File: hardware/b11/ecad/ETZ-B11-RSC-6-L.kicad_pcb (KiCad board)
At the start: 2 copper layers, 112.3 x 85.8 mm, 0 parts

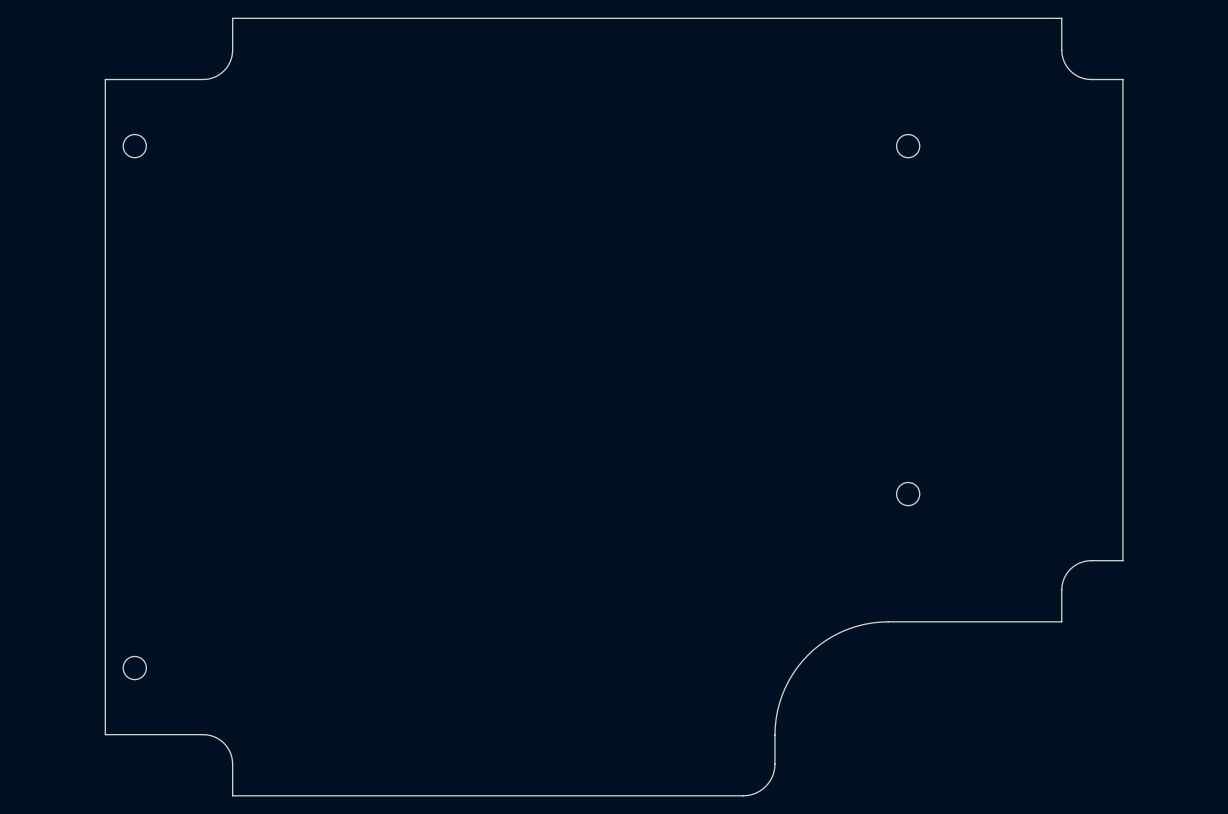
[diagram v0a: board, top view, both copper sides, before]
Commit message: fix(hardware/b11): correct 6-col PCB outlines and regenerate all boards
Update DXF outlines for all 6-col variants (LSC, RSC, LSP, RSP — both
normal and low profile) exported manually from OnShape with the _6
configuration. Regenerate all 16 KiCad PCBs from the corrected outlines
and re-place MX hotswap switches on the 4 normal-profile carrier boards.

Co-Authored-By: Claude Sonnet 4.6 <noreply@anthropic.com>
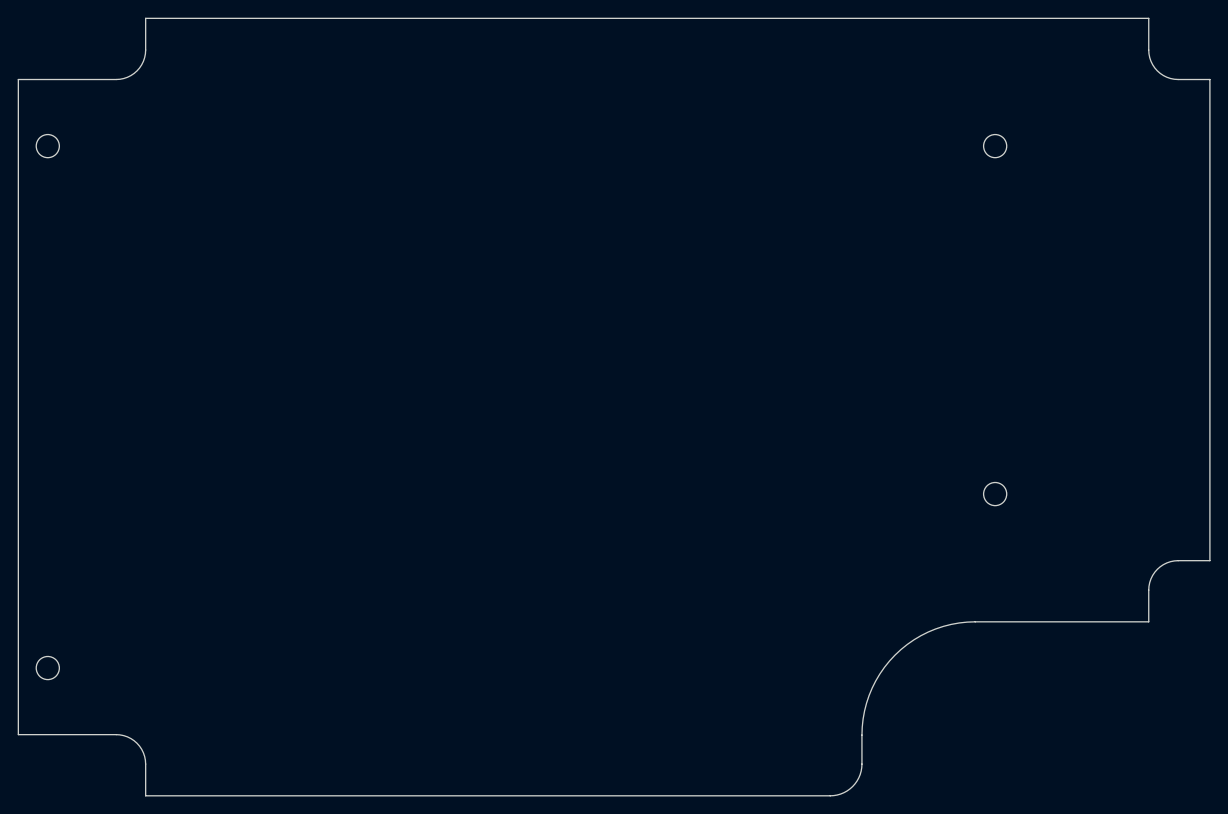
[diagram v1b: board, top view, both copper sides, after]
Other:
- board size 112.3 x 85.8 mm -> 131.5 x 85.8 mm
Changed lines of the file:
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@@
 		(allow_soldermask_bridges_in_footprints no)
 		(tenting front back)
-		(grid_origin 190.55 73.3)
+		(grid_origin 200.15 73.3)
 		(pcbplotparams
 			(layerselection 0x00000000_00000000_55555555_5755f5ff)
@@
 	)
 	(net 0 "")
-	(gr_circle
-		(center 180.949999 111.7)
-		(end 182.224999 111.7)
-		(stroke
-			(width 0.05)
-			(type default)
-		)
-		(fill no)
-		(layer "Edge.Cuts")
-	)
-	(gr_line
-		(start 106.399999 59.2)
-		(end 197.899999 59.2)
-		(stroke
-			(width 0.05)
-			(type default)
-		)
-		(layer "Edge.Cuts")
-	)
-	(gr_line
-		(start 204.65 65.95)
-		(end 204.65 119.05)
-		(stroke
-			(width 0.05)
-			(type default)
-		)
-		(layer "Edge.Cuts")
-	)
-	(gr_line
-		(start 197.899999 122.3)
-		(end 197.899999 125.8)
-		(stroke
-			(width 0.05)
-			(type default)
-		)
-		(layer "Edge.Cuts")
-	)
-	(gr_line
-		(start 103.15 138.25)
-		(end 92.35 138.25)
-		(stroke
-			(width 0.05)
-			(type default)
-		)
-		(layer "Edge.Cuts")
-	)
-	(gr_arc
-		(start 197.899999 122.3)
-		(mid 198.851902 120.001903)
-		(end 201.149999 119.05)
-		(stroke
-			(width 0.05)
-			(type default)
-		)
-		(layer "Edge.Cuts")
-	)
-	(gr_line
-		(start 92.35 138.25)
-		(end 92.35 65.95)
-		(stroke
-			(width 0.05)
-			(type default)
-		)
-		(layer "Edge.Cuts")
-	)
-	(gr_line
-		(start 201.149999 65.95)
-		(end 204.65 65.95)
-		(stroke
-			(width 0.05)
-			(type default)
-		)
-		(layer "Edge.Cuts")
-	)
-	(gr_arc
-		(start 106.4 62.7)
-		(mid 105.448097 64.998097)
-		(end 103.15 65.95)
-		(stroke
-			(width 0.05)
-			(type default)
-		)
-		(layer "Edge.Cuts")
-	)
-	(gr_line
-		(start 166.249999 138.3)
-		(end 166.249999 141.5)
-		(stroke
-			(width 0.05)
-			(type default)
-		)
-		(layer "Edge.Cuts")
-	)
-	(gr_line
-		(start 201.149999 119.05)
-		(end 204.65 119.05)
-		(stroke
-			(width 0.05)
-			(type default)
-		)
-		(layer "Edge.Cuts")
-	)
-	(gr_arc
-		(start 166.249999 141.5)
-		(mid 165.224873 143.974874)
-		(end 162.749999 145)
-		(stroke
-			(width 0.05)
-			(type default)
-		)
-		(layer "Edge.Cuts")
-	)
-	(gr_circle
-		(center 95.6 73.3)
-		(end 96.874999 73.3)
-		(stroke
-			(width 0.05)
-			(type default)
-		)
-		(fill no)
-		(layer "Edge.Cuts")
-	)
-	(gr_line
-		(start 162.749999 145)
-		(end 106.399999 145)
-		(stroke
-			(width 0.05)
-			(type default)
-		)
-		(layer "Edge.Cuts")
-	)
-	(gr_arc
-		(start 103.15 138.25)
-		(mid 105.448097 139.201903)
-		(end 106.4 141.5)
-		(stroke
-			(width 0.05)
-			(type default)
-		)
-		(layer "Edge.Cuts")
-	)
-	(gr_arc
-		(start 166.249999 138.3)
-		(mid 169.911164 129.461165)
-		(end 178.749999 125.8)
-		(stroke
-			(width 0.05)
-			(type default)
-		)
-		(layer "Edge.Cuts")
-	)
-	(gr_circle
-		(center 95.6 130.9)
-		(end 96.874999 130.9)
-		(stroke
-			(width 0.05)
-			(type default)
-		)
-		(fill no)
-		(layer "Edge.Cuts")
-	)
-	(gr_line
-		(start 197.899999 125.8)
-		(end 178.749999 125.8)
-		(stroke
-			(width 0.05)
-			(type default)
-		)
-		(layer "Edge.Cuts")
-	)
-	(gr_line
-		(start 106.399999 62.7)
-		(end 106.399999 59.2)
-		(stroke
-			(width 0.05)
-			(type default)
-		)
-		(layer "Edge.Cuts")
-	)
-	(gr_line
-		(start 197.899999 62.7)
-		(end 197.899999 59.2)
-		(stroke
-			(width 0.05)
-			(type default)
-		)
-		(layer "Edge.Cuts")
-	)
-	(gr_line
-		(start 103.15 65.95)
-		(end 92.35 65.95)
-		(stroke
-			(width 0.05)
-			(type default)
-		)
-		(layer "Edge.Cuts")
-	)
-	(gr_circle
-		(center 180.949999 73.3)
-		(end 182.224999 73.3)
-		(stroke
-			(width 0.05)
-			(type default)
-		)
-		(fill no)
-		(layer "Edge.Cuts")
-	)
-	(gr_line
-		(start 106.399999 141.5)
-		(end 106.399999 145)
-		(stroke
-			(width 0.05)
-			(type default)
-		)
-		(layer "Edge.Cuts")
-	)
-	(gr_arc
-		(start 201.149999 65.95)
-		(mid 198.851902 64.998097)
-		(end 197.899999 62.7)
-		(stroke
-			(width 0.05)
+	(gr_line
+		(start 207.5 125.799999)
+		(end 188.349999 125.799999)
+		(stroke
+			(width 0.05)
+			(type default)
+		)
+		(layer "Edge.Cuts")
+	)
+	(gr_line
+		(start 175.849999 138.3)
+		(end 175.849999 141.5)
+		(stroke
+			(width 0.05)
+			(type default)
+		)
+		(layer "Edge.Cuts")
+	)
+	(gr_arc
+		(start 210.75 65.95)
+		(mid 208.451903 64.998097)
+		(end 207.5 62.7)
+		(stroke
+			(width 0.05)
+			(type default)
+		)
+		(layer "Edge.Cuts")
+	)
+	(gr_arc
+		(start 93.55 138.25)
+		(mid 95.848097 139.201903)
+		(end 96.8 141.5)
+		(stroke
+			(width 0.05)
+			(type default)
+		)
+		(layer "Edge.Cuts")
+	)
+	(gr_line
+		(start 214.25 65.95)
+		(end 214.25 119.05)
+		(stroke
+			(width 0.05)
+			(type default)
+		)
+		(layer "Edge.Cuts")
+	)
+	(gr_circle
+		(center 190.55 111.7)
+		(end 191.825 111.7)
+		(stroke
+			(width 0.05)
+			(type default)
+		)
+		(fill no)
+		(layer "Edge.Cuts")
+	)
+	(gr_line
+		(start 82.75 138.25)
+		(end 82.75 65.95)
+		(stroke
+			(width 0.05)
+			(type default)
+		)
+		(layer "Edge.Cuts")
+	)
+	(gr_line
+		(start 96.8 59.199999)
+		(end 207.5 59.2)
+		(stroke
+			(width 0.05)
+			(type default)
+		)
+		(layer "Edge.Cuts")
+	)
+	(gr_line
+		(start 93.55 138.25)
+		(end 82.75 138.25)
+		(stroke
+			(width 0.05)
+			(type default)
+		)
+		(layer "Edge.Cuts")
+	)
+	(gr_line
+		(start 210.75 119.05)
+		(end 214.25 119.05)
+		(stroke
+			(width 0.05)
+			(type default)
+		)
+		(layer "Edge.Cuts")
+	)
+	(gr_line
+		(start 207.5 62.7)
+		(end 207.5 59.2)
+		(stroke
+			(width 0.05)
+			(type default)
+		)
+		(layer "Edge.Cuts")
+	)
+	(gr_line
+		(start 96.8 62.7)
+		(end 96.8 59.199999)
+		(stroke
+			(width 0.05)
+			(type default)
+		)
+		(layer "Edge.Cuts")
+	)
+	(gr_line
+		(start 96.8 141.5)
+		(end 96.8 145)
+		(stroke
+			(width 0.05)
+			(type default)
+		)
+		(layer "Edge.Cuts")
+	)
+	(gr_line
+		(start 93.55 65.95)
+		(end 82.75 65.95)
+		(stroke
+			(width 0.05)
+			(type default)
+		)
+		(layer "Edge.Cuts")
+	)
+	(gr_arc
+		(start 175.849999 138.3)
+		(mid 179.511164 129.461165)
+		(end 188.349999 125.8)
+		(stroke
+			(width 0.05)
+			(type default)
+		)
+		(layer "Edge.Cuts")
+	)
+	(gr_circle
+		(center 190.55 73.3)
+		(end 191.825 73.3)
+		(stroke
+			(width 0.05)
+			(type default)
+		)
+		(fill no)
+		(layer "Edge.Cuts")
+	)
+	(gr_line
+		(start 210.75 65.95)
+		(end 214.25 65.95)
+		(stroke
+			(width 0.05)
+			(type default)
+		)
+		(layer "Edge.Cuts")
+	)
+	(gr_arc
+		(start 96.8 62.7)
+		(mid 95.848097 64.998097)
+		(end 93.55 65.95)
+		(stroke
+			(width 0.05)
+			(type default)
+		)
+		(layer "Edge.Cuts")
+	)
+	(gr_line
+		(start 207.5 122.3)
+		(end 207.5 125.799999)
+		(stroke
+			(width 0.05)
+			(type default)
+		)
+		(layer "Edge.Cuts")
+	)
+	(gr_line
+		(start 172.349999 145)
+		(end 96.8 145)
+		(stroke
+			(width 0.05)
+			(type default)
+		)
+		(layer "Edge.Cuts")
+	)
+	(gr_arc
+		(start 207.5 122.3)
+		(mid 208.451903 120.001903)
+		(end 210.75 119.05)
+		(stroke
+			(width 0.05)
+			(type default)
+		)
+		(layer "Edge.Cuts")
+	)
+	(gr_circle
+		(center 86 130.9)
+		(end 87.274999 130.9)
+		(stroke
+			(width 0.05)
+			(type default)
+		)
+		(fill no)
+		(layer "Edge.Cuts")
+	)
+	(gr_circle
+		(center 86 73.3)
+		(end 87.274999 73.3)
+		(stroke
+			(width 0.05)
+			(type default)
+		)
+		(fill no)
+		(layer "Edge.Cuts")
+	)
+	(gr_arc
+		(start 175.849999 141.5)
+		(mid 174.824873 143.974874)
+		(end 172.349999 145)
+		(stroke
+			(width 0.05)

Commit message: feat(hardware/b11): place hotswap sockets on all carrier boards, south-facing
- Place Kailh MX hotswap sockets (MX-Hotswap-1U) on 4 normal-profile carrier
  boards at 19.2mm pitch, flipped to B.Cu, 180° south-facing orientation
- Place Kailh Choc v1 hotswap sockets (PG1350) on 4 low-profile carrier boards
  at 19.2mm pitch, 180° south-facing orientation
- Add 3D model (Kailh-Choc-Socket-CPG135001S30.step) to PG1350 footprint with
  correct offset/rotation for B.Cu-pad, F.Cu-module placement
- Strip F.SilkS, F.Fab, F.CrtYd top-layer graphics from LP carrier PG1350 footprints
- Rename place-b11-switches.py → place-b11-switches-np.py for symmetry with new lp script
- Add place-b11-switches-lp.py for Choc v1 placement automation

Co-Authored-By: Claude Sonnet 4.6 <noreply@anthropic.com>
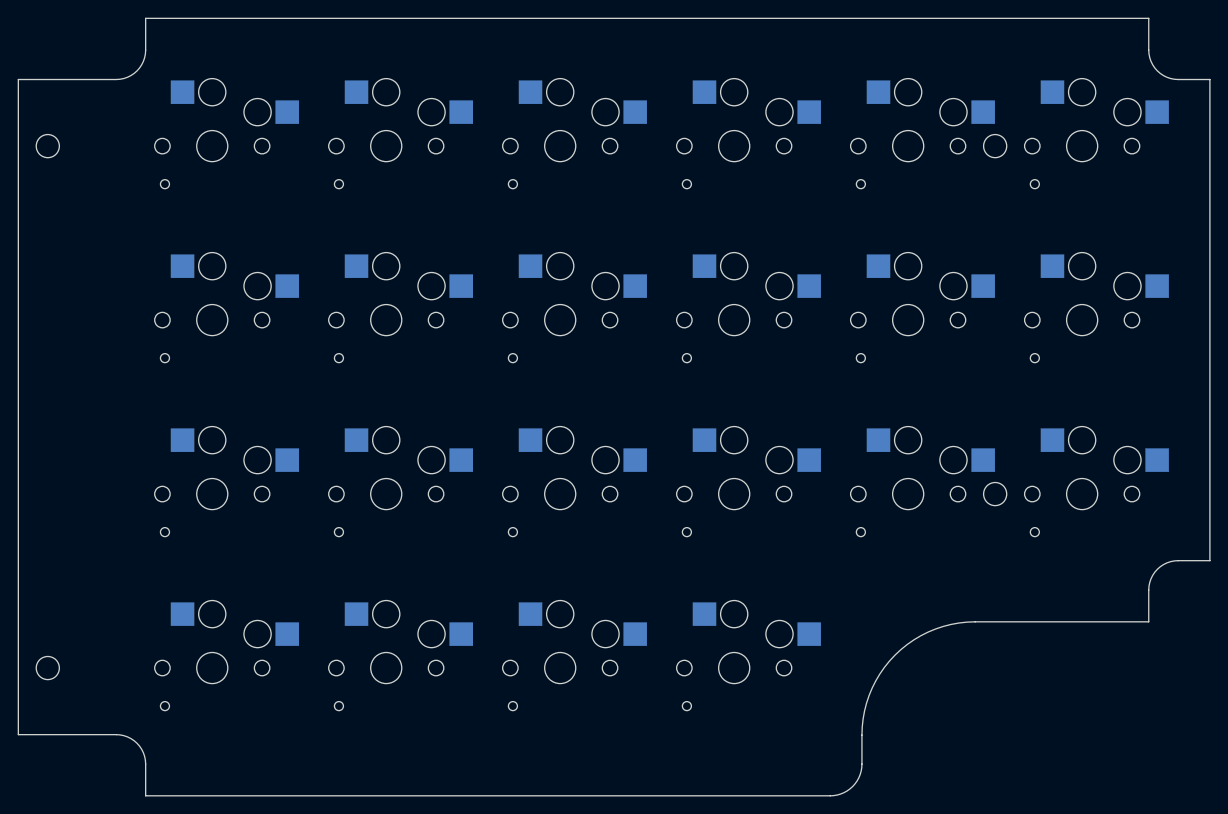
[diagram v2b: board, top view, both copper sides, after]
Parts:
- added SW1: Kailh_socket_PG1350, Kailh_socket_PG1350, F.Cu at (200.2, 73.3)
- added SW10: Kailh_socket_PG1350, Kailh_socket_PG1350, F.Cu at (142.6, 92.5)
- added SW11: Kailh_socket_PG1350, Kailh_socket_PG1350, F.Cu at (123.3, 92.5)
- added SW12: Kailh_socket_PG1350, Kailh_socket_PG1350, F.Cu at (104.2, 92.5)
- added SW13: Kailh_socket_PG1350, Kailh_socket_PG1350, F.Cu at (200.2, 111.7)
- added SW14: Kailh_socket_PG1350, Kailh_socket_PG1350, F.Cu at (180.9, 111.7)
- added SW15: Kailh_socket_PG1350, Kailh_socket_PG1350, F.Cu at (161.8, 111.7)
- added SW16: Kailh_socket_PG1350, Kailh_socket_PG1350, F.Cu at (142.6, 111.7)
- added SW17: Kailh_socket_PG1350, Kailh_socket_PG1350, F.Cu at (123.3, 111.7)
- added SW18: Kailh_socket_PG1350, Kailh_socket_PG1350, F.Cu at (104.2, 111.7)
- added SW19: Kailh_socket_PG1350, Kailh_socket_PG1350, F.Cu at (161.8, 130.9)
- added SW2: Kailh_socket_PG1350, Kailh_socket_PG1350, F.Cu at (180.9, 73.3)
- added SW20: Kailh_socket_PG1350, Kailh_socket_PG1350, F.Cu at (142.6, 130.9)
- added SW21: Kailh_socket_PG1350, Kailh_socket_PG1350, F.Cu at (123.3, 130.9)
- added SW22: Kailh_socket_PG1350, Kailh_socket_PG1350, F.Cu at (104.2, 130.9)
- added SW3: Kailh_socket_PG1350, Kailh_socket_PG1350, F.Cu at (161.8, 73.3)
- added SW4: Kailh_socket_PG1350, Kailh_socket_PG1350, F.Cu at (142.6, 73.3)
- added SW5: Kailh_socket_PG1350, Kailh_socket_PG1350, F.Cu at (123.3, 73.3)
- added SW6: Kailh_socket_PG1350, Kailh_socket_PG1350, F.Cu at (104.2, 73.3)
- added SW7: Kailh_socket_PG1350, Kailh_socket_PG1350, F.Cu at (200.2, 92.5)
- added SW8: Kailh_socket_PG1350, Kailh_socket_PG1350, F.Cu at (180.9, 92.5)
- added SW9: Kailh_socket_PG1350, Kailh_socket_PG1350, F.Cu at (161.8, 92.5)

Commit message: feat(hardware/b11): add SMD 6028 back-mount LED footprint and place on all carrier PCBs
- Add LED_SMD_6028_BackMount footprint with router-safe rounded-rectangle
  slot cutout (3.3 × 3.9 mm, 0.5 mm corners, 1 mm bit), roundrect pads
  (1.4 × 2.8 mm, 25% ratio), silkscreen polarity markers clear of pads
- Add LED_SMD_6028.step 3D model from 3D Content Central
- Add place-b11-leds.py: places 18–22 LEDs per carrier PCB aligned to
  the switch grid, 5.9 mm south of each switch center
- Place LEDs on all 8 carrier PCBs (LSC/RSC × 5/6-col × N/L)

Co-Authored-By: Claude Sonnet 4.6 <noreply@anthropic.com>
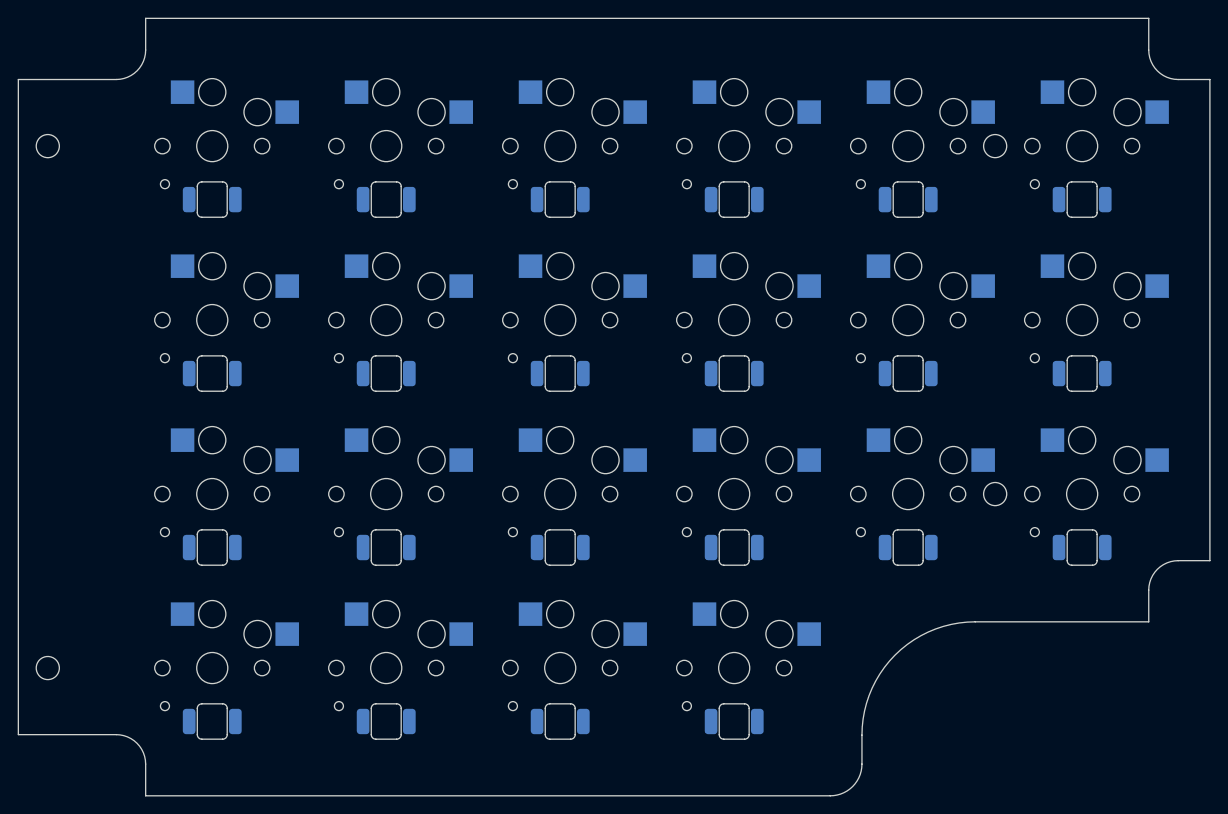
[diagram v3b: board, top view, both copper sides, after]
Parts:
- added LED1: LED_SMD_6028_BackMount, LED_SMD_6028_BackMount, B.Cu at (200.2, 79.2)
- added LED10: LED_SMD_6028_BackMount, LED_SMD_6028_BackMount, B.Cu at (142.6, 98.4)
- added LED11: LED_SMD_6028_BackMount, LED_SMD_6028_BackMount, B.Cu at (123.3, 98.4)
- added LED12: LED_SMD_6028_BackMount, LED_SMD_6028_BackMount, B.Cu at (104.2, 98.4)
- added LED13: LED_SMD_6028_BackMount, LED_SMD_6028_BackMount, B.Cu at (200.2, 117.6)
- added LED14: LED_SMD_6028_BackMount, LED_SMD_6028_BackMount, B.Cu at (180.9, 117.6)
- added LED15: LED_SMD_6028_BackMount, LED_SMD_6028_BackMount, B.Cu at (161.8, 117.6)
- added LED16: LED_SMD_6028_BackMount, LED_SMD_6028_BackMount, B.Cu at (142.6, 117.6)
- added LED17: LED_SMD_6028_BackMount, LED_SMD_6028_BackMount, B.Cu at (123.3, 117.6)
- added LED18: LED_SMD_6028_BackMount, LED_SMD_6028_BackMount, B.Cu at (104.2, 117.6)
- added LED19: LED_SMD_6028_BackMount, LED_SMD_6028_BackMount, B.Cu at (161.8, 136.8)
- added LED2: LED_SMD_6028_BackMount, LED_SMD_6028_BackMount, B.Cu at (180.9, 79.2)
- added LED20: LED_SMD_6028_BackMount, LED_SMD_6028_BackMount, B.Cu at (142.6, 136.8)
- added LED21: LED_SMD_6028_BackMount, LED_SMD_6028_BackMount, B.Cu at (123.3, 136.8)
- added LED22: LED_SMD_6028_BackMount, LED_SMD_6028_BackMount, B.Cu at (104.2, 136.8)
- added LED3: LED_SMD_6028_BackMount, LED_SMD_6028_BackMount, B.Cu at (161.8, 79.2)
- added LED4: LED_SMD_6028_BackMount, LED_SMD_6028_BackMount, B.Cu at (142.6, 79.2)
- added LED5: LED_SMD_6028_BackMount, LED_SMD_6028_BackMount, B.Cu at (123.3, 79.2)
- added LED6: LED_SMD_6028_BackMount, LED_SMD_6028_BackMount, B.Cu at (104.2, 79.2)
- added LED7: LED_SMD_6028_BackMount, LED_SMD_6028_BackMount, B.Cu at (200.2, 98.4)
- added LED8: LED_SMD_6028_BackMount, LED_SMD_6028_BackMount, B.Cu at (180.9, 98.4)
- added LED9: LED_SMD_6028_BackMount, LED_SMD_6028_BackMount, B.Cu at (161.8, 98.4)
